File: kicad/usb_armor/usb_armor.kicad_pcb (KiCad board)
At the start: 2 copper layers, 29 x 29 mm, 16 parts, among them J1 USB, J2 USB

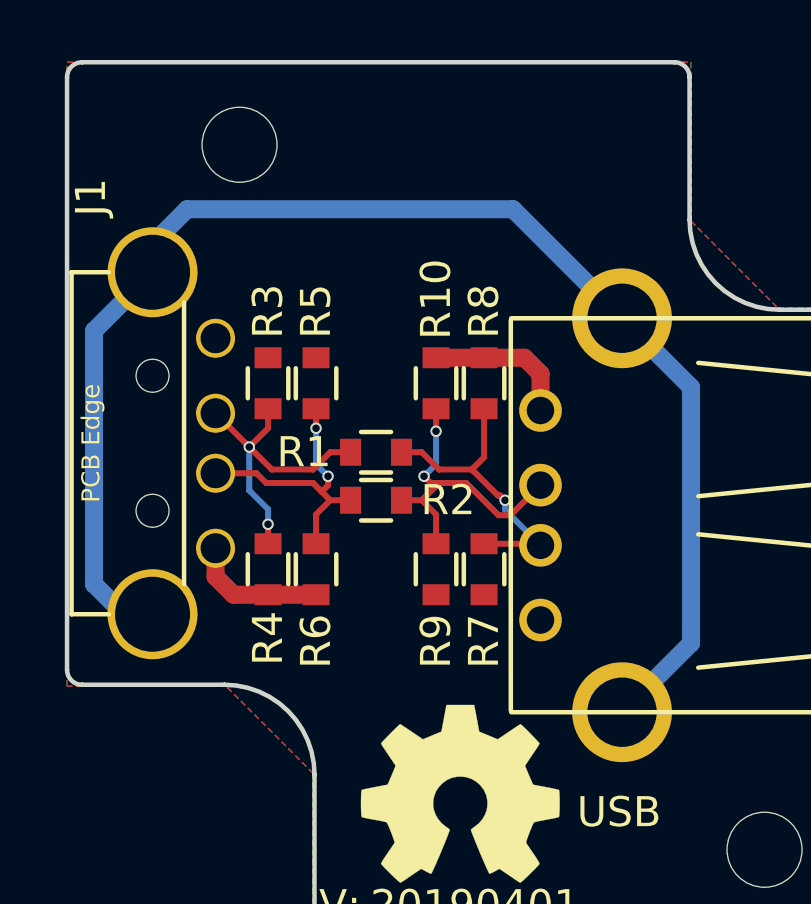
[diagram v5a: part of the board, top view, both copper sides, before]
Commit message: added some capacitors and a power led
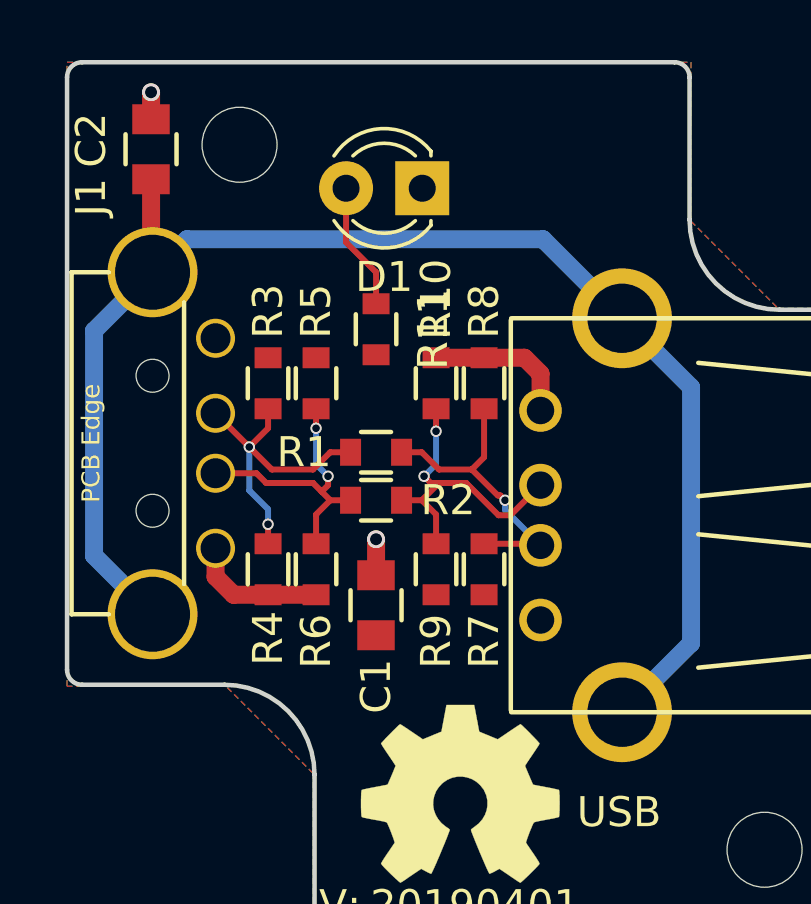
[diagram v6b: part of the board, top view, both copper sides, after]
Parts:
- added C1: 1u, SquantorRcl:C_0805, F.Cu at (143.7, 104.9)
- added C2: 100n, SquantorRcl:C_0805, F.Cu at (136.2, 89.7)
- added D1: LED, LED_THT:LED_D3.0mm, F.Cu at (145.2, 91.0)
- added R11: 1K, SquantorRcl:R_0603_hand, F.Cu at (143.7, 95.7)
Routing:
- net Net-(D1-Pad2): track 0.00 -> 4.26 mm
- net /GND: track 9.48 -> 11.6 mm, vias 0 -> 2
- net /Shield: track 47.2 -> 48.4 mm
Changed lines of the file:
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@@
     (thickness 1.6)
     (drawings 16)
-    (tracks 75)
+    (tracks 83)
     (zones 0)
-    (modules 16)
-    (nets 8)
+    (modules 20)
+    (nets 9)
   )
   (page A4)
@@
   )
   (setup
-    (last_trace_width 0.6)
+    (last_trace_width 0.2)
     (user_trace_width 0.1524)
     (user_trace_width 0.2)
@@
   (net 6 /OUT_USB-D+)
   (net 7 /OUT_USB-D-)
+  (net 8 "Net-(D1-Pad2)")
   (net_class Default "This is the default net class."
     (clearance 0.1524)
@@
     (add_net /Shield)
     (add_net /VBUS)
+    (add_net "Net-(D1-Pad2)")
+  )
+  (module SquantorRcl:C_0805 (layer F.Cu)
+    (at 136.2 89.7 270)
+    (descr "Capacitor SMD 0805, reflow soldering, AVX (see smccp.pdf)")
+    (tags "capacitor 0805")
+    (attr smd)
+    (fp_text reference C2 (at -0.3 2 270) (layer F.SilkS)
+      (effects (font (size 1 1) (thickness 0.15)))
+    )
+    (fp_text value 100n (at 0 2.1 270) (layer F.Fab)
+      (effects (font (size 1 1) (thickness 0.15)))
+    )
+    (fp_line (start -0.5 0.85) (end 0.5 0.85) (layer F.SilkS) (width 0.15))
+    (fp_line (start 0.5 -0.85) (end -0.5 -0.85) (layer F.SilkS) (width 0.15))
+    (fp_line (start 1.8 -1) (end 1.8 1) (layer F.CrtYd) (width 0.05))
+    (fp_line (start -1.8 -1) (end -1.8 1) (layer F.CrtYd) (width 0.05))
+    (fp_line (start -1.8 1) (end 1.8 1) (layer F.CrtYd) (width 0.05))
+    (fp_line (start -1.8 -1) (end 1.8 -1) (layer F.CrtYd) (width 0.05))
+    (fp_line (start -1 -0.625) (end 1 -0.625) (layer F.Fab) (width 0.15))
+    (fp_line (start 1 -0.625) (end 1 0.625) (layer F.Fab) (width 0.15))
+    (fp_line (start 1 0.625) (end -1 0.625) (layer F.Fab) (width 0.15))
+    (fp_line (start -1 0.625) (end -1 -0.625) (layer F.Fab) (width 0.15))
+    (pad 2 smd rect (at 1 0 270) (size 1 1.25) (layers F.Cu F.Paste F.Mask)
+      (net 3 /Shield))
+    (pad 1 smd rect (at -1 0 270) (size 1 1.25) (layers F.Cu F.Paste F.Mask)
+      (net 2 /GND))
+    (model Capacitors_SMD.3dshapes/C_0805.wrl
+      (at (xyz 0 0 0))
+      (scale (xyz 1 1 1))
+      (rotate (xyz 0 0 0))
+    )
+  )
+  (module SquantorRcl:R_0603_hand (layer F.Cu)
+    (at 143.7 95.7 270)
+    (descr "Resistor SMD 0603, reflow soldering, Vishay (see dcrcw.pdf)")
+    (tags "resistor 0603")
+    (attr smd)
+    (fp_text reference R11 (at 0 -1.9 270) (layer F.SilkS)
+      (effects (font (size 1 1) (thickness 0.15)))
+    )
+    (fp_text value 1K (at 0 1.9 270) (layer F.Fab)
+      (effects (font (size 1 1) (thickness 0.15)))
+    )
+    (fp_line (start -0.5 -0.675) (end 0.5 -0.675) (layer F.SilkS) (width 0.15))
+    (fp_line (start 0.5 0.675) (end -0.5 0.675) (layer F.SilkS) (width 0.15))
+    (fp_line (start 1.5 -0.8) (end 1.5 0.8) (layer F.CrtYd) (width 0.05))
+    (fp_line (start -1.5 -0.8) (end -1.5 0.8) (layer F.CrtYd) (width 0.05))
+    (fp_line (start -1.5 0.8) (end 1.5 0.8) (layer F.CrtYd) (width 0.05))
+    (fp_line (start -1.5 -0.8) (end 1.5 -0.8) (layer F.CrtYd) (width 0.05))
+    (fp_line (start -0.8 -0.4) (end 0.8 -0.4) (layer F.Fab) (width 0.1))
+    (fp_line (start 0.8 -0.4) (end 0.8 0.4) (layer F.Fab) (width 0.1))
+    (fp_line (start 0.8 0.4) (end -0.8 0.4) (layer F.Fab) (width 0.1))
+    (fp_line (start -0.8 0.4) (end -0.8 -0.4) (layer F.Fab) (width 0.1))
+    (pad 2 smd rect (at 0.85 0 270) (size 0.7 0.9) (layers F.Cu F.Paste F.Mask)
+      (net 1 /VBUS))
+    (pad 1 smd rect (at -0.85 0 270) (size 0.7 0.9) (layers F.Cu F.Paste F.Mask)
+      (net 8 "Net-(D1-Pad2)"))
+    (model Resistors_SMD.3dshapes/R_0603.wrl
+      (at (xyz 0 0 0))
+      (scale (xyz 1 1 1))
+      (rotate (xyz 0 0 0))
+    )
+  )
+  (module LED_THT:LED_D3.0mm (layer F.Cu)
+    (at 145.24 91 180)
+    (descr "LED, diameter 3.0mm, 2 pins")
+    (tags "LED diameter 3.0mm 2 pins")
+    (fp_text reference D1 (at 1.27 -2.96 180) (layer F.SilkS)
+      (effects (font (size 1 1) (thickness 0.15)))
+    )
+    (fp_text value LED (at 1.27 2.96 180) (layer F.Fab)
+      (effects (font (size 1 1) (thickness 0.15)))
+    )
+    (fp_line (start 3.7 -2.25) (end -1.15 -2.25) (layer F.CrtYd) (width 0.05))
+    (fp_line (start 3.7 2.25) (end 3.7 -2.25) (layer F.CrtYd) (width 0.05))
+    (fp_line (start -1.15 2.25) (end 3.7 2.25) (layer F.CrtYd) (width 0.05))
+    (fp_line (start -1.15 -2.25) (end -1.15 2.25) (layer F.CrtYd) (width 0.05))
+    (fp_line (start -0.29 1.08) (end -0.29 1.236) (layer F.SilkS) (width 0.12))
+    (fp_line (start -0.29 -1.236) (end -0.29 -1.08) (layer F.SilkS) (width 0.12))
+    (fp_line (start -0.23 -1.16619) (end -0.23 1.16619) (layer F.Fab) (width 0.1))
+    (fp_circle (center 1.27 0) (end 2.77 0) (layer F.Fab) (width 0.1))
+    (fp_arc (start 1.27 0) (end 0.229039 1.08) (angle -87.9) (layer F.SilkS) (width 0.12))
+    (fp_arc (start 1.27 0) (end 0.229039 -1.08) (angle 87.9) (layer F.SilkS) (width 0.12))
+    (fp_arc (start 1.27 0) (end -0.29 1.235516) (angle -108.8) (layer F.SilkS) (width 0.12))
+    (fp_arc (start 1.27 0) (end -0.29 -1.235516) (angle 108.8) (layer F.SilkS) (width 0.12))
+    (fp_arc (start 1.27 0) (end -0.23 -1.16619) (angle 284.3) (layer F.Fab) (width 0.1))
+    (pad 2 thru_hole circle (at 2.54 0 180) (size 1.8 1.8) (drill 0.9) (layers *.Cu *.Mask)
+      (net 8 "Net-(D1-Pad2)"))
+    (pad 1 thru_hole rect (at 0 0 180) (size 1.8 1.8) (drill 0.9) (layers *.Cu *.Mask)
+      (net 2 /GND))
+    (model ${KISYS3DMOD}/LED_THT.3dshapes/LED_D3.0mm.wrl
+      (at (xyz 0 0 0))
+      (scale (xyz 1 1 1))
+      (rotate (xyz 0 0 0))
+    )
+  )
+  (module SquantorRcl:C_0805 (layer F.Cu)
+    (at 143.7 104.9 270)
+    (descr "Capacitor SMD 0805, reflow soldering, AVX (see smccp.pdf)")
+    (tags "capacitor 0805")
+    (attr smd)
+    (fp_text reference C1 (at 2.7 0 270) (layer F.SilkS)
+      (effects (font (size 1 1) (thickness 0.15)))
+    )
+    (fp_text value 1u (at 2.7 0 270) (layer F.Fab)
+      (effects (font (size 1 1) (thickness 0.15)))
+    )
+    (fp_line (start -0.5 0.85) (end 0.5 0.85) (layer F.SilkS) (width 0.15))
+    (fp_line (start 0.5 -0.85) (end -0.5 -0.85) (layer F.SilkS) (width 0.15))
+    (fp_line (start 1.8 -1) (end 1.8 1) (layer F.CrtYd) (width 0.05))
+    (fp_line (start -1.8 -1) (end -1.8 1) (layer F.CrtYd) (width 0.05))
+    (fp_line (start -1.8 1) (end 1.8 1) (layer F.CrtYd) (width 0.05))
+    (fp_line (start -1.8 -1) (end 1.8 -1) (layer F.CrtYd) (width 0.05))
+    (fp_line (start -1 -0.625) (end 1 -0.625) (layer F.Fab) (width 0.15))
+    (fp_line (start 1 -0.625) (end 1 0.625) (layer F.Fab) (width 0.15))
+    (fp_line (start 1 0.625) (end -1 0.625) (layer F.Fab) (width 0.15))
+    (fp_line (start -1 0.625) (end -1 -0.625) (layer F.Fab) (width 0.15))
+    (pad 2 smd rect (at 1 0 270) (size 1 1.25) (layers F.Cu F.Paste F.Mask)
+      (net 1 /VBUS))
+    (pad 1 smd rect (at -1 0 270) (size 1 1.25) (layers F.Cu F.Paste F.Mask)
+      (net 2 /GND))
+    (model Capacitors_SMD.3dshapes/C_0805.wrl
+      (at (xyz 0 0 0))
+      (scale (xyz 1 1 1))
+      (rotate (xyz 0 0 0))
+    )
   )
   (module SquantorRcl:R_0603_hand (layer F.Cu)
@@
   (segment (start 149.1822 97.1822) (end 149.1822 98.4075) (width 0.6) (layer F.Cu) (net 2))
   (segment (start 148.65 96.65) (end 149.1822 97.1822) (width 0.6) (layer F.Cu) (net 2))
-  (segment (start 136.25 105.2) (end 135.3 105.2) (width 0.6) (layer B.Cu) (net 3))
-  (segment (start 135.3 105.2) (end 134.3 104.2) (width 0.6) (layer B.Cu) (net 3))
-  (segment (start 134.3 95.75) (end 136.25 93.8) (width 0.6) (layer B.Cu) (net 3))
-  (segment (start 134.3 104.2) (end 134.3 95.75) (width 0.6) (layer B.Cu) (net 3))
-  (segment (start 136.25 93.8) (end 136.25 92.85) (width 0.6) (layer B.Cu) (net 3))
-  (segment (start 136.25 92.85) (end 137.4 91.7) (width 0.6) (layer B.Cu) (net 3))
-  (segment (start 148.2659 91.7) (end 151.9 95.3341) (width 0.6) (layer B.Cu) (net 3))
-  (segment (start 137.4 91.7) (end 148.2659 91.7) (width 0.6) (layer B.Cu) (net 3))
+  (via (at 136.2 87.8) (size 0.6) (drill 0.4) (layers F.Cu B.Cu) (net 2))
+  (segment (start 136.2 88.7) (end 136.2 87.8) (width 0.6) (layer F.Cu) (net 2))
+  (via (at 143.7 102.7) (size 0.6) (drill 0.4) (layers F.Cu B.Cu) (net 2))
+  (segment (start 143.7 103.9) (end 143.7 102.7) (width 0.6) (layer F.Cu) (net 2))
   (segment (start 151.9 95.3341) (end 154.2 97.6341) (width 0.6) (layer B.Cu) (net 3))
   (segment (start 154.2 106.1659) (end 151.9 108.4659) (width 0.6) (layer B.Cu) (net 3))
   (segment (start 154.2 97.6341) (end 154.2 106.1659) (width 0.6) (layer B.Cu) (net 3))
+  (segment (start 134.3 95.75) (end 136.25 93.8) (width 0.6) (layer B.Cu) (net 3))
+  (segment (start 136.25 105.2) (end 134.3 103.25) (width 0.6) (layer B.Cu) (net 3))
+  (segment (start 134.3 103.25) (end 134.3 95.75) (width 0.6) (layer B.Cu) (net 3))
+  (segment (start 136.2 93.75) (end 136.25 93.8) (width 0.6) (layer F.Cu) (net 3))
+  (segment (start 136.2 90.7) (end 136.2 93.75) (width 0.6) (layer F.Cu) (net 3))
+  (segment (start 149.2659 92.7) (end 151.9 95.3341) (width 0.6) (layer B.Cu) (net 3))
+  (segment (start 137.4 92.7) (end 149.2659 92.7) (width 0.6) (layer B.Cu) (net 3))
+  (segment (start 136.25 93.8) (end 136.3 93.8) (width 0.6) (layer B.Cu) (net 3))
+  (segment (start 136.3 93.8) (end 137.4 92.7) (width 0.6) (layer B.Cu) (net 3))
   (segment (start 142.174999 99.8) (end 142.85 99.8) (width 0.2) (layer F.Cu) (net 4))
   (segment (start 141.599999 100.375) (end 142.174999 99.8) (width 0.2) (layer F.Cu) (net 4))
@@
   (segment (start 149.1289 102.85) (end 149.1822 102.9033) (width 0.2) (layer F.Cu) (net 7))
   (segment (start 147.3 102.85) (end 149.1289 102.85) (width 0.2) (layer F.Cu) (net 7))
+  (segment (start 143.7 94.85) (end 143.7 93.8) (width 0.2) (layer F.Cu) (net 8))
+  (segment (start 142.7 92.8) (end 142.7 91) (width 0.2) (layer F.Cu) (net 8))
+  (segment (start 143.7 93.8) (end 142.7 92.8) (width 0.2) (layer F.Cu) (net 8))
   (zone (net 2) (net_name /GND) (layer B.Cu) (hatch edge 0.508)
     (connect_pads (clearance 0.508))

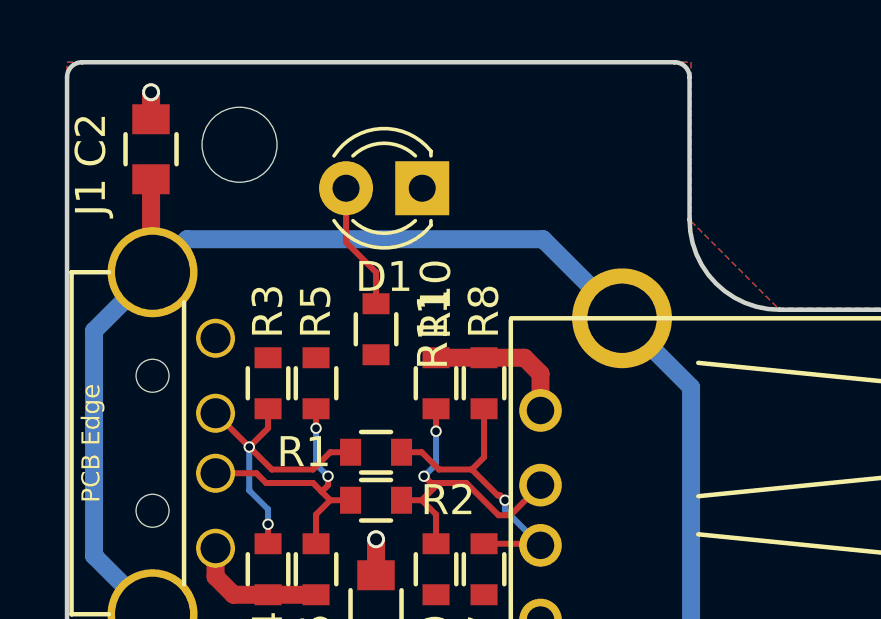
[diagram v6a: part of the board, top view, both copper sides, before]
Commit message: silk placement improved
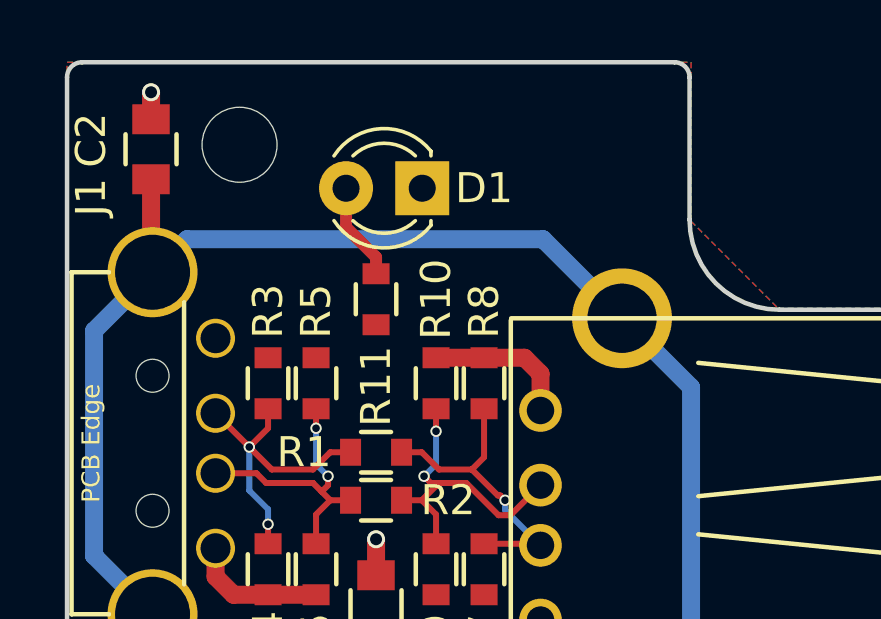
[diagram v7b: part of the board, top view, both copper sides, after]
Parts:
- moved R11 1.00 mm to (143.7, 94.7)
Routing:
- net Net-(D1-Pad2): track 4.26 -> 3.26 mm
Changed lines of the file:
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@@
   )
   (setup
-    (last_trace_width 0.2)
+    (last_trace_width 0.4)
     (user_trace_width 0.1524)
     (user_trace_width 0.2)
@@
   )
   (module SquantorRcl:R_0603_hand (layer F.Cu)
-    (at 143.7 95.7 270)
-    (descr "Resistor SMD 0603, reflow soldering, Vishay (see dcrcw.pdf)")
-    (tags "resistor 0603")
-    (attr smd)
-    (fp_text reference R11 (at 0 -1.9 270) (layer F.SilkS)
-      (effects (font (size 1 1) (thickness 0.15)))
-    )
-    (fp_text value 1K (at 0 1.9 270) (layer F.Fab)
+    (at 143.7 94.7 270)
+    (descr "Resistor SMD 0603, reflow soldering, Vishay (see dcrcw.pdf)")
+    (tags "resistor 0603")
+    (attr smd)
+    (fp_text reference R11 (at 2.9 0 270) (layer F.SilkS)
+      (effects (font (size 1 1) (thickness 0.15)))
+    )
+    (fp_text value 1K (at 3 0 270) (layer F.Fab)
       (effects (font (size 1 1) (thickness 0.15)))
     )
@@
     (descr "LED, diameter 3.0mm, 2 pins")
     (tags "LED diameter 3.0mm 2 pins")
-    (fp_text reference D1 (at 1.27 -2.96 180) (layer F.SilkS)
-      (effects (font (size 1 1) (thickness 0.15)))
-    )
-    (fp_text value LED (at 1.27 2.96 180) (layer F.Fab)
+    (fp_text reference D1 (at -2.06 0 180) (layer F.SilkS)
+      (effects (font (size 1 1) (thickness 0.15)))
+    )
+    (fp_text value LED (at -2.46 0 180) (layer F.Fab)
       (effects (font (size 1 1) (thickness 0.15)))
     )
@@
   (segment (start 149.1289 102.85) (end 149.1822 102.9033) (width 0.2) (layer F.Cu) (net 7))
   (segment (start 147.3 102.85) (end 149.1289 102.85) (width 0.2) (layer F.Cu) (net 7))
-  (segment (start 143.7 94.85) (end 143.7 93.8) (width 0.2) (layer F.Cu) (net 8))
-  (segment (start 142.7 92.8) (end 142.7 91) (width 0.2) (layer F.Cu) (net 8))
-  (segment (start 143.7 93.8) (end 142.7 92.8) (width 0.2) (layer F.Cu) (net 8))
+  (segment (start 142.7 91) (end 142.7 92.3) (width 0.4) (layer F.Cu) (net 8))
+  (segment (start 143.7 93.3) (end 143.7 93.85) (width 0.4) (layer F.Cu) (net 8))
+  (segment (start 142.7 92.3) (end 143.7 93.3) (width 0.4) (layer F.Cu) (net 8))
   (zone (net 2) (net_name /GND) (layer B.Cu) (hatch edge 0.508)
     (connect_pads (clearance 0.508))
